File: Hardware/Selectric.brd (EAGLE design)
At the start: 101.5 x 53.3 mm, 57 parts, among them IC1 MAX3232ESE, IC2 UDN2982SLW, IC3 UDN2982SLW

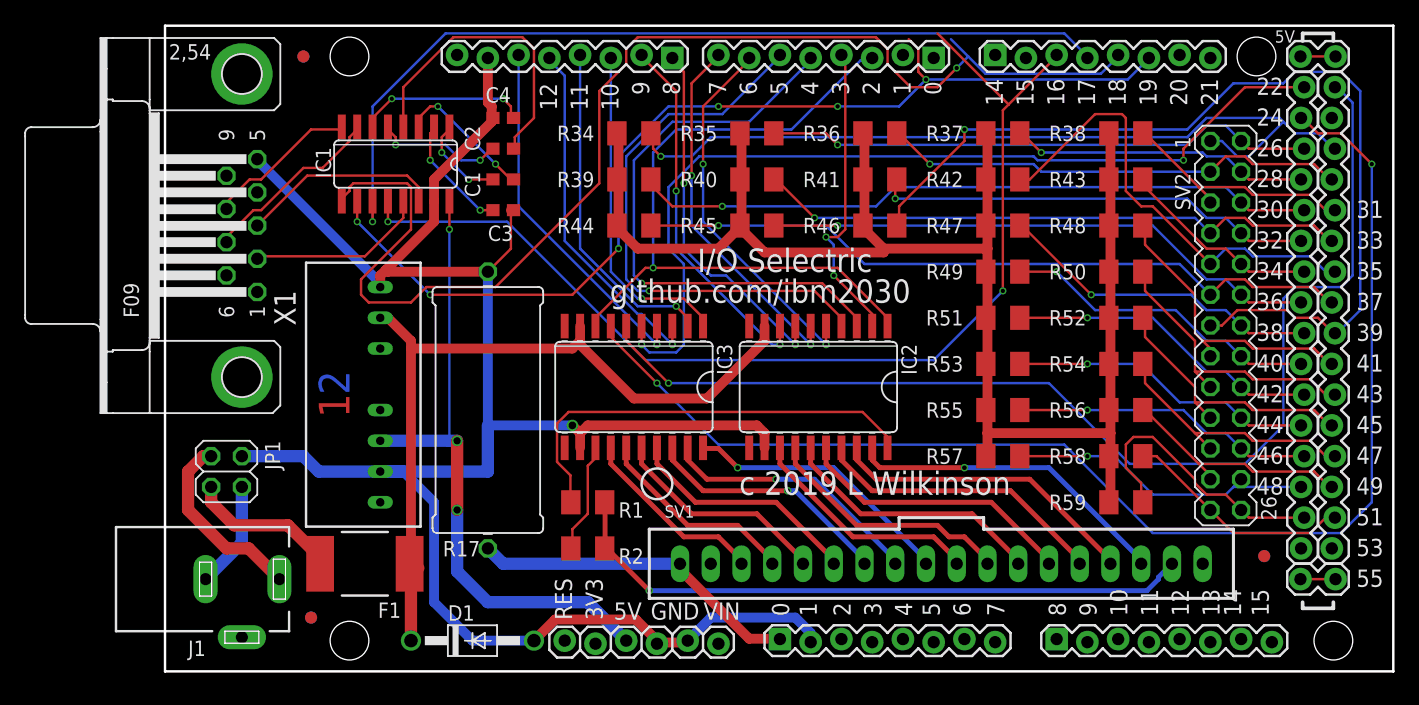
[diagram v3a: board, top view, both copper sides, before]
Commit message: Add switch/LED header J2
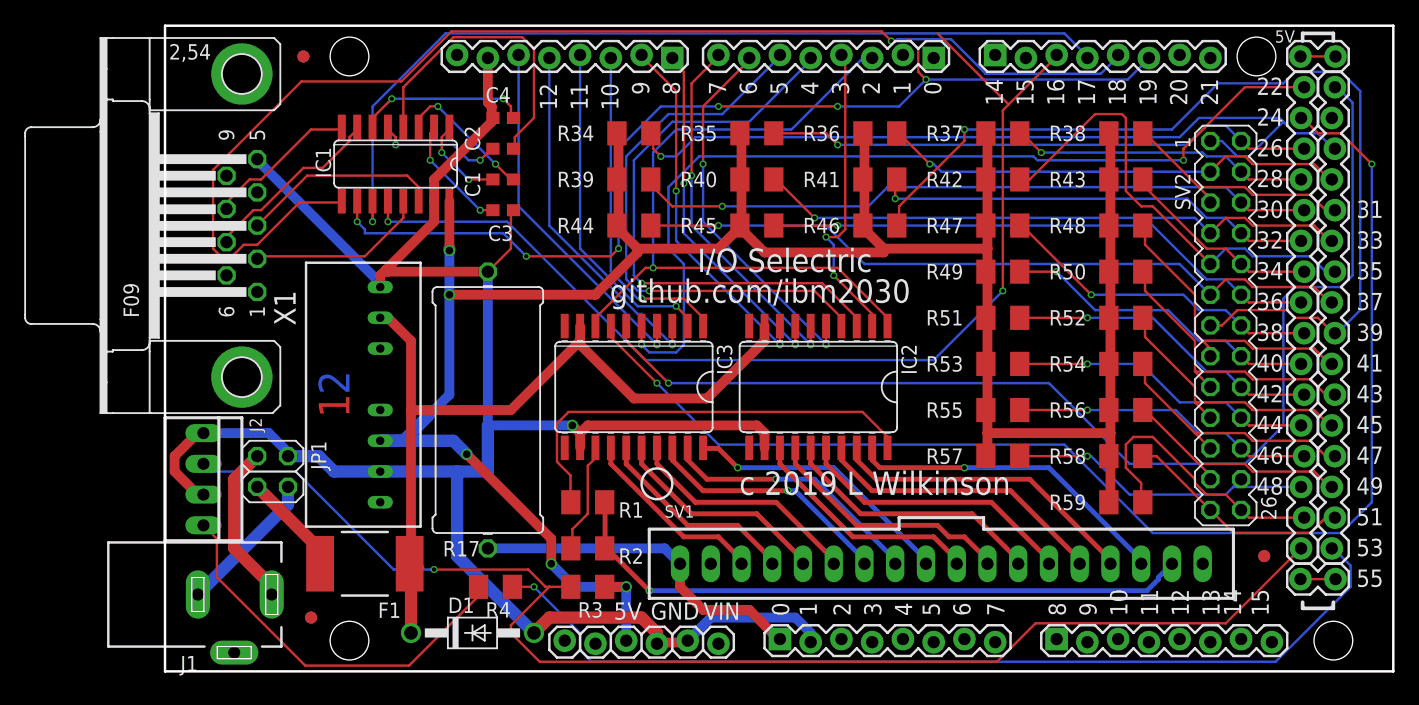
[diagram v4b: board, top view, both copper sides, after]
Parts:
- added J2: 22-23-2041, con-molex:22-23-2041
- added R3, R4: 220R, rcl:M1206
- moved JP1 3.81 mm to (8.89, 16.5)
- moved J1 1.42 mm to (5.71, 6.35)
- moved D1 0.63 mm to (25.4, 3.17)
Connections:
- removed net 5V: DC1.6, IC1.16, JP10.3
- new net LED+: J2.4, R4.2
- net D52: now also J2.2, R3.2
- net D53: now also R4.1
- net GND: now also J2.1, J2.3
- net VCC: now also DC1.6, IC1.16, JP10.3, R3.1
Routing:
- net D52: track 0.00 -> 109.8 mm, vias 0 -> 1
- net D53: track 0.00 -> 79.1 mm, vias 0 -> 1
- net VCC: track 130.2 -> 203.8 mm, vias 0 -> 5
- net 5V: track 53.3 -> 0.00 mm, vias 3 -> 0
- net LED+: track 0.00 -> 32.6 mm
- net GND: track 165.9 -> 170.5 mm
- net N$42: track 12.7 -> 8.50 mm
- net N$23: track 8.86 -> 12.0 mm
- net TX2: track 86.1 -> 84.0 mm
- net N$24: track 15.5 -> 13.5 mm
- net HSDCOM: track 66.7 -> 68.2 mm
- net D8: track 30.2 -> 29.4 mm
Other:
- board text removed: "3V3"
- board text removed: "RES"

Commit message: Finalise components and values. add BoM
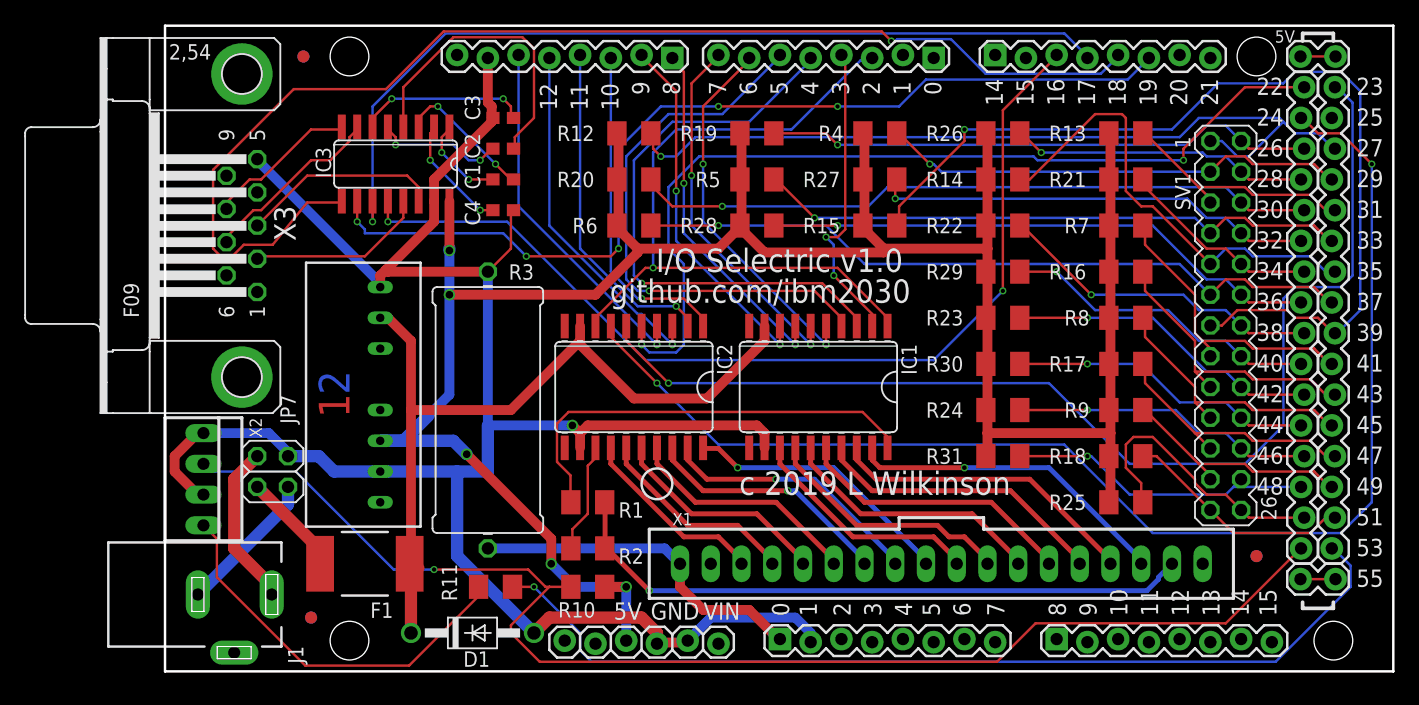
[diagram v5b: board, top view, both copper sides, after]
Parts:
- removed JP12: (no value), SparkFun:1X02_LOCK
- removed R36, R54: 220R, rcl:M1206
- removed SV2: (no value), con-lstb:MA13-2
- added JP2: M16LOCK, SparkFun:1X16_LOCK
- added R10: 1K, rcl:M1206
- added R11: 220R, rcl:M1206
- added X3: (no value), con-subd:F09HP
- DC1: value TMR -> TMR1-4811
- IC1: value MAX3232ESE -> UDN2982SLW; device maxim:SO16 -> uln-udn:SO20W
- IC3: value UDN2982SLW -> MAX3232ESE; device uln-udn:SO20W -> maxim:SO16
- JP1: value (none) -> M16LOCK; device pinhead:2X02 -> SparkFun:1X16_LOCK
- JP10: device SparkFun:1X06_LOCK -> SparkFun:1X08_LOCK
- JP11: device SparkFun:1X02_LOCK -> SparkFun:1X08_LOCK
- JP3, JP4: device SparkFun:1X08_LOCK -> SparkFun:1X02_LOCK
- JP5: device SparkFun:1X08_LOCK -> SparkFun:1X06_LOCK
- JP7: device SparkFun:1X08_LOCK -> pinhead:2X02
- JP8, JP9: value M16LOCK -> (none); device SparkFun:1X16_LOCK -> SparkFun:1X08_LOCK
- R12, R13, R14, R15, R16, R18, R19, R20, R21, R22, R23, R24, R25, R26, R27, R28, R29, R30, R31, R4, R5, R6, R7, R8, R9: value 220R -> 1K
- R17: value 1R0 -> 1K; device rcl:0922/22 -> rcl:M1206
- R3: value 220R -> 1R0; device rcl:M1206 -> rcl:0922/22
- SV1: value C-GRID-18-70543 -> (none); device con-molex:70543-18 -> con-lstb:MA13-2
- X1: value (none) -> C-GRID-18-70543; device con-subd:F09HP -> con-molex:70543-18
- moved JP1 87.9 mm to (96.5, 10.2), turned to 90 degrees
- moved X1 64.2 mm to (64.1, 8.89), turned to 180 degrees
- moved JP5 59.9 mm to (33.0, 2.54)
- moved JP6 57.8 mm to (41.9, 50.8), turned to 180 degrees
- moved JP4 52.9 mm to (94.0, 7.62), turned to 0 degrees
- moved R17 52.8 mm to (79.4, 25.4), turned to 0 degrees
- moved JP3 52.1 mm to (94.0, 50.8), turned to 0 degrees
- moved JP11 50.1 mm to (68.6, 50.8)
- moved R4 49.1 mm to (59.1, 44.5), turned to 0 degrees
- moved JP8 46.4 mm to (50.8, 2.54), turned to 0 degrees
- moved JP7 44.2 mm to (8.89, 16.5), turned to 270 degrees
- moved JP10 40.6 mm to (73.7, 2.54)
- moved IC1 39.5 mm to (54.0, 23.5)
- moved SV1 30.7 mm to (87.6, 28.6), turned to 270 degrees
- moved JP9 30.6 mm to (63.5, 50.8), turned to 180 degrees
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- renumbered J2 to X2, R34 to R12, R35 to R19, R37 to R26, R38 to R13, R39 to R20, R40 to R5, R41 to R27, R42 to R14, R43 to R21, R44 to R6, R45 to R28, R46 to R15, R47 to R22, R48 to R7, R49 to R29, R50 to R16, R51 to R23, R52 to R8, R53 to R30, R55 to R24, R56 to R9, R57 to R31, R58 to R18, R59 to R25
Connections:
- net 3.3: now also JP5.2; no longer JP10.2
- net 5V@1: now also JP3.1, JP3.2; no longer JP12.1, JP12.2
- net A10: now also JP10.3; no longer JP6.3
- net A11: now also JP10.4; no longer JP6.4
- net A12: now also JP10.5; no longer JP6.5
- net A13: now also JP10.6; no longer JP6.6
- net A14: now also JP10.7; no longer JP6.7
- net A15: now also JP10.8; no longer JP6.8
- net A2: now also JP8.3; no longer JP7.3
- net A3: now also JP8.4; no longer JP7.4
- net A4: now also JP8.5; no longer JP7.5
- net A5: now also JP8.6; no longer JP7.6
- net A6: now also JP8.7; no longer JP7.7
- net A7: now also JP8.8; no longer JP7.8
- net A8: now also JP10.1; no longer JP6.1
- net A9: now also JP10.2; no longer JP6.2
- net AREF: now also JP6.8; no longer JP3.8
- net CTS: now also IC3.8, X3.8; no longer IC1.8, X1.8
- net D10: now also IC2.1, JP6.3; no longer IC3.1, JP3.3
- net D11: now also IC2.2, JP6.4; no longer IC3.2, JP3.4
- net D12: now also IC2.3, JP6.5; no longer IC3.3, JP3.5
- net D13: now also IC2.4, JP6.6; no longer IC3.4, JP3.6
- net D14: now also JP11.8; no longer JP5.8
- net D15: now also JP11.7; no longer JP5.7
- net D2: now also IC1.1, IC2.8, JP9.3; no longer IC2.1, IC3.8, JP4.3
- net D22: now also IC2.5, JP2.1; no longer IC3.5, JP9.1
- net D23: now also IC2.6, JP1.16; no longer IC3.6, JP8.16
- net D24: now also IC2.7, JP2.2; no longer IC3.7, JP9.2
- net D25: now also JP1.15; no longer JP8.15
- net D26: now also JP2.3, SV1.2; no longer JP9.3, SV2.2
- net D27: now also JP1.14, SV1.1; no longer JP8.14, SV2.1
- net D28: now also JP2.4, SV1.4; no longer JP9.4, SV2.4
- net D29: now also JP1.13, R4.2, SV1.3; no longer JP8.13, R36.2, SV2.3
- net D3: now also IC1.2, JP9.4; no longer IC2.2, JP4.4
- net D30: now also JP2.5, SV1.6; no longer JP9.5, SV2.6
- net D31: now also JP1.12, SV1.5; no longer JP8.12, SV2.5
- net D32: now also JP2.6, SV1.8; no longer JP9.6, SV2.8
- net D33: now also JP1.11, SV1.7; no longer JP8.11, SV2.7
- net D34: now also JP2.7, SV1.10; no longer JP9.7, SV2.10
- net D35: now also JP1.10, SV1.9; no longer JP8.10, SV2.9
- net D36: now also JP2.8, SV1.12; no longer JP9.8, SV2.12
- net D37: now also JP1.9, SV1.11; no longer JP8.9, SV2.11
- net D38: now also JP2.9, SV1.14; no longer JP9.9, SV2.14
- net D39: now also JP1.8, SV1.13; no longer JP8.8, SV2.13
- net D4: now also IC1.3, JP9.5; no longer IC2.3, JP4.5
- net D40: now also JP2.10, SV1.16; no longer JP9.10, SV2.16
- net D41: now also JP1.7, SV1.15; no longer JP8.7, SV2.15
- net D42: now also JP2.11, SV1.18; no longer JP9.11, SV2.18
- net D43: now also JP1.6, SV1.17; no longer JP8.6, SV2.17
- net D44: now also JP2.12, SV1.20; no longer JP9.12, SV2.20
- net D45: now also JP1.5, SV1.19; no longer JP8.5, SV2.19
- net D46: now also JP2.13, SV1.22; no longer JP9.13, SV2.22
- net D47: now also JP1.4, R17.2, SV1.21; no longer JP8.4, R54.2, SV2.21
- net D48: now also JP2.14, SV1.24; no longer JP9.14, SV2.24
- net D49: now also JP1.3, SV1.23; no longer JP8.3, SV2.23
- net D5: now also IC1.4, JP9.6; no longer IC2.4, JP4.6
- net D50: now also JP2.15, SV1.26; no longer JP9.15, SV2.26
- net D51: now also JP1.2, SV1.25; no longer JP8.2, SV2.25
- net D52: now also JP2.16, R10.2; no longer JP9.16, R3.2
- net D53: now also JP1.1, R11.1; no longer JP8.1, R4.1
- net D6: now also IC1.5, JP9.7; no longer IC2.5, JP4.7
- net D7: now also IC1.6, JP9.8; no longer IC2.6, JP4.8
- net D8: now also IC1.7, JP6.1; no longer IC2.7, JP3.1
- net D9: now also IC1.8, JP6.2; no longer IC2.8, JP3.2
- net GND: now also IC1.12, IC3.15, JP5.4, JP5.5, JP6.7, JP8.2, R3.1, X3.5; no longer IC1.15, IC3.12, JP1.2, JP10.4, JP10.5, JP3.7, R17.1, X1.5
- net HSD1: now also X1.2; no longer SV1.2
- net HSD10: now also IC2.19, X1.11; no longer IC3.19, SV1.11
- net HSD11: now also IC2.18, X1.12; no longer IC3.18, SV1.12
- net HSD12: now also IC2.17, X1.13; no longer IC3.17, SV1.13
- net HSD13: now also IC2.16, X1.14; no longer IC3.16, SV1.14
- net HSD14: now also IC2.15, X1.15; no longer IC3.15, SV1.15
- net HSD15: now also IC2.14, X1.16; no longer IC3.14, SV1.16
- net HSD16: now also X1.17; no longer SV1.17
- net HSD2: now also IC1.19, X1.3; no longer IC2.19, SV1.3
- net HSD3: now also IC1.18, X1.4; no longer IC2.18, SV1.4
- net HSD4: now also IC1.17, X1.5; no longer IC2.17, SV1.5
- net HSD5: now also IC1.16, X1.6; no longer IC2.16, SV1.6
- net HSD6: now also IC1.15, X1.7; no longer IC2.15, SV1.7
- net HSD7: now also IC1.14, X1.8; no longer IC2.14, SV1.8
- net HSD8: now also IC1.13, X1.9; no longer IC2.13, SV1.9
- net HSD9: now also IC2.20, X1.10; no longer IC3.20, SV1.10
- net HSDCOM: now also IC1.9; no longer IC3.9
- net HSDRET: now also JP8.1, R3.2, X1.18; no longer JP7.1, R17.2, SV1.18
- net IN_GND: now also JP4.1, JP4.2; no longer JP11.1, JP11.2
- net LED+: now also R11.2; no longer R4.2
- net N$1: now also IC3.1; no longer IC1.1
- net N$2: now also IC3.4; no longer IC1.4
- net N$23: now also JP7.4; no longer JP1.4
- net N$24: now also JP7.1; no longer JP1.1
- net N$3: now also IC3.3; no longer IC1.3
- net N$4: now also IC3.5; no longer IC1.5
- net N$42: now also JP7.3; no longer JP1.3
- net N$5: now also IC2.13; no longer IC3.13
- net N$6: now also C4.1, IC3.2; no longer C3.1, IC1.2
- net N$7: now also C3.1, IC3.6; no longer C4.1, IC1.6
- net N$8: now also IC1.20; no longer IC2.20
- net RES: now also JP5.1; no longer JP10.1
- net RTS: now also IC3.7, X3.7; no longer IC1.7, X1.7
- net RX0: now also JP9.1; no longer JP4.1
- net RX1: now also IC3.12, JP11.3; no longer IC1.12, JP5.3
- net RX2: now also IC3.9, JP11.5; no longer IC1.9, JP5.5
- net RXD: now also IC3.13, X3.2; no longer IC1.13, X1.2
- net SCL: now also JP11.1; no longer JP5.1
- net SDA: now also JP11.2; no longer JP5.2
- net TX0: now also JP9.2; no longer JP4.2
- net TX1: now also IC3.11, JP11.4; no longer IC1.11, JP5.4
- net TX2: now also IC3.10, JP11.6; no longer IC1.10, JP5.6
- net TXD: now also IC3.14, X3.3; no longer IC1.14, X1.3
- net VCC: now also IC3.16, JP5.3, R10.1, R17.1, R4.1; no longer IC1.16, JP10.3, R3.1, R36.1, R54.1
- net VIN: now also JP5.6; no longer JP10.6
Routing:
- net RX1: track 89.2 -> 80.9 mm
- net TX2: track 84.0 -> 80.1 mm, vias 6 -> 5
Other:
- board text added: "23"
- board text added: "25"
- board text added: "27"
- board text added: "29"
- board text added: "I/O Selectric v1.0"
- board text removed: "I/O Selectric"

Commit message: Modify connectors, assign I/Os
Add eC-stencil registration holes
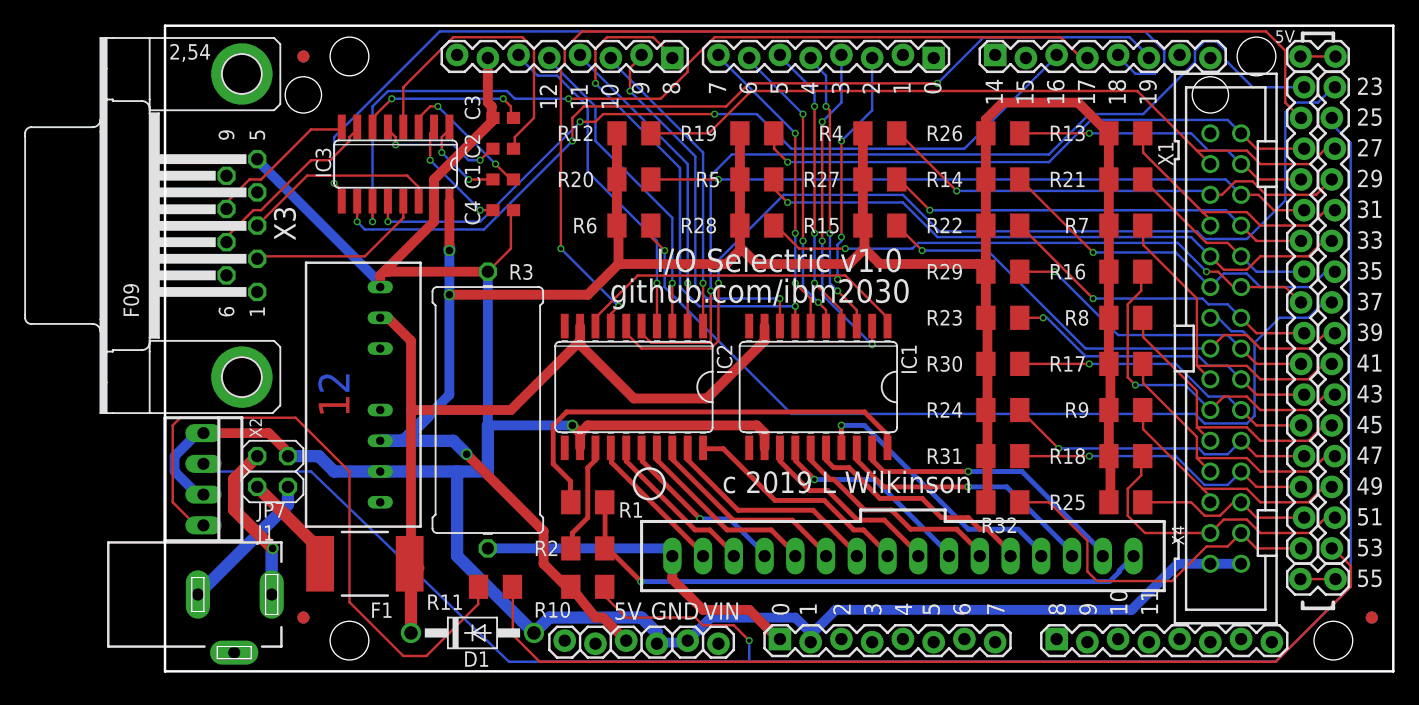
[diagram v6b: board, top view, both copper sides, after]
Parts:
- removed SV1: (no value), con-lstb:MA13-2
- added R32: 1K, rcl:M1206
- added X4: C-GRID-16-70543, con-molex:70543-16
- R11: value 220R -> 1K
- X1: value C-GRID-18-70543 -> 2530-; device con-molex:70543-18 -> con-3m:PAK100/2500-30
- moved X1 29.5 mm to (87.6, 26.7), turned to 270 degrees
- moved U$2 10.8 mm to (99.7, 4.45)
- moved U$1 0.63 mm to (11.4, 4.45)
- turned R10 to 0 degrees
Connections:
- removed net HSD16: X1.17
- net D25: now also R10.2, X2.2
- net D26: now also X1.2; no longer SV1.2
- net D27: now also X1.3; no longer SV1.1
- net D28: now also X1.4; no longer SV1.4
- net D29: now also X1.5; no longer SV1.3
- net D30: now also X1.6; no longer SV1.6
- net D31: now also X1.7; no longer SV1.5
- net D32: now also X1.8; no longer SV1.8
- net D33: now also X1.9; no longer SV1.7
- net D34: now also X1.10; no longer SV1.10
- net D35: now also X1.11; no longer SV1.9
- net D36: now also X1.12; no longer SV1.12
- net D37: now also X1.13; no longer SV1.11
- net D38: now also X1.14; no longer SV1.14
- net D39: now also X1.15; no longer SV1.13
- net D40: now also X1.16; no longer SV1.16
- net D41: now also X1.17; no longer SV1.15
- net D42: now also X1.18; no longer SV1.18
- net D43: now also X1.19; no longer SV1.17
- net D44: now also X1.20; no longer SV1.20
- net D45: now also X1.21; no longer SV1.19
- net D46: now also X1.22; no longer SV1.22
- net D47: now also X1.23; no longer SV1.21
- net D48: now also X1.24; no longer SV1.24
- net D49: now also X1.25; no longer SV1.23
- net D50: now also X1.26; no longer SV1.26
- net D51: now also X1.27; no longer SV1.25
- net D52: now also R32.1, X1.28; no longer R10.2, X2.2
- net GND: now also X1.29, X1.30
- net HSD1: now also X4.1; no longer X1.2
- net HSD10: now also X4.10; no longer X1.11
- net HSD11: now also X4.11; no longer X1.12
- net HSD12: now also X4.12; no longer X1.13
- net HSD13: now also X4.13; no longer X1.14
- net HSD14: now also X4.14; no longer X1.15
- net HSD15: now also X4.15; no longer X1.16
- net HSD2: now also X4.2; no longer X1.3
- net HSD3: now also X4.3; no longer X1.4
- net HSD4: now also X4.4; no longer X1.5
- net HSD5: now also X4.5; no longer X1.6
- net HSD6: now also X4.6; no longer X1.7
- net HSD7: now also X4.7; no longer X1.8
- net HSD8: now also X4.8; no longer X1.9
- net HSD9: now also X4.9; no longer X1.10
- net HSDRET: now also X4.16; no longer X1.18
- net VCC: now also R32.2
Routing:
- net D25: track 0.00 -> 159.6 mm, vias 0 -> 1
- net D52: track 109.8 -> 29.6 mm, vias 1 -> 0
- net GND: track 170.5 -> 209.0 mm
- net D39: track 78.3 -> 41.8 mm
- net D4: track 48.3 -> 23.7 mm, vias 1 -> 3
- net D5: track 46.2 -> 24.5 mm, vias 1 -> 3
- net LED+: track 32.6 -> 52.9 mm
- net D37: track 59.9 -> 77.5 mm
- net RX2: track 101.4 -> 84.5 mm
- net RX1: track 80.9 -> 65.1 mm, vias 2 -> 3
- net D24: track 106.9 -> 92.2 mm
- net D23: track 94.3 -> 79.8 mm
- net D8: track 29.4 -> 41.9 mm
- net D2: track 59.9 -> 48.2 mm, vias 1 -> 3
- net D50: track 23.4 -> 14.9 mm
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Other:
- board text removed: "13"
- board text removed: "20"
- board text removed: "21"
- board text removed: "22"
- board text removed: "24"
- board text removed: "26"
- board text removed: "28"
- board text removed: "30"
- board text removed: "32"
- board text removed: "34"
- board text removed: "36"
- board text removed: "38"
- board text removed: "40"
- board text removed: "42"
- board text removed: "44"
- board text removed: "46"
- board text removed: "48"

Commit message: Version as ordered
Note BoM is not necessarily accurate
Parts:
- added HSD1A: (no value), wirepad:2,15/1,0
- added R33: 1K, rcl:M1206
- moved JP11 17.8 mm to (86.4, 50.8), turned to 180 degrees
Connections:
- net N$5 renamed HSD1A
- net D15: now also R33.1, X1.1
- net HSD1: now also HSD1A.1
- net VCC: now also R33.2
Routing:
- net HSD1: track 49.7 -> 116.2 mm, vias 1 -> 2
- net D15: track 0.00 -> 22.5 mm
- net TX2: track 75.8 -> 96.1 mm, vias 3 -> 0
- net RX2: track 84.5 -> 72.4 mm
- net D24: track 92.2 -> 104.1 mm, vias 2 -> 3
- net RX1: track 65.1 -> 76.0 mm, vias 3 -> 1
- net GND: track 209.0 -> 217.4 mm
- net TX1: track 74.3 -> 68.8 mm
- net D53: track 80.6 -> 75.1 mm
- net D22: track 76.6 -> 72.8 mm, vias 1 -> 2
- net LED+: track 52.9 -> 49.1 mm
- net HSDCOM: track 68.2 -> 66.2 mm
- net D25: track 159.6 -> 159.0 mm
- net VCC: track 206.4 -> 207.0 mm, vias 3 -> 2
- net D27: track 62.6 -> 62.7 mm, vias 0 -> 1
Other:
- board text removed: "18"
- board text removed: "19"
